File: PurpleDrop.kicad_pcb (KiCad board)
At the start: 4 copper layers, 161 x 92 mm, 145 parts, among them J1 Conn_02x32_Odd_Even, J2 Conn_02x32_Odd_Even, J3 Conn_02x20_Odd_Even, J4 Conn_01x04, J5 Conn_01x04, J6 Conn_01x04, J7 Conn_02x04_Odd_Even, J8 Conn_02x10_Odd_Even, J9 Barrel_Jack_Switch, Q1 SSM3K329R, Q2 SSM3K329R, Q3 SSM3K329R, Q4 SSM3K329R, SW1 SW_SPDT, U1 HV507, U10 RRE04EA6DFH, U11 RRE04EA6DFH, U12 RRE04EA6DFH, U13 RRE04EA6DFH, U14 RRE04EA6DFH, U15 RRE04EA6DFH, U16 RRE04EA6DFH, U17 RRE04EA6DFH, U18 RRE04EA6DFH, U19 RRE04EA6DFH, U2 HV507, U20 RRE04EA6DFH, U21 RRE04EA6DFH, U22 RRE04EA6DFH, U23 RRE04EA6DFH, U24 RRE04EA6DFH, U25 RRE04EA6DFH, U26 RRE04EA6DFH, U27 RRE04EA6DFH, U28 RRE04EA6DFH, U29 RRE04EA6DFH, U3 RRE04EA6DFH, U30 RRE04EA6DFH, U31 RRE04EA6DFH, U32 RRE04EA6DFH, U33 RRE04EA6DFH, U34 RRE04EA6DFH, U35 RRE04EA6DFH, U36 RRE04EA6DFH, U37 RRE04EA6DFH, U38 RRE04EA6DFH, U39 RRE04EA6DFH, U4 RRE04EA6DFH, U40 RRE04EA6DFH, U41 RRE04EA6DFH, U42 RRE04EA6DFH, U43 RRE04EA6DFH, U44 RRE04EA6DFH, U45 RRE04EA6DFH, U46 RRE04EA6DFH, U47 RRE04EA6DFH, U48 RRE04EA6DFH, U49 RRE04EA6DFH, U5 RRE04EA6DFH, U50 RRE04EA6DFH, U51 RRE04EA6DFH, U52 RRE04EA6DFH, U53 RRE04EA6DFH, U54 RRE04EA6DFH, U55 RRE04EA6DFH, U56 RRE04EA6DFH, U57 RRE04EA6DFH, U58 RRE04EA6DFH, U59 RRE04EA6DFH, U6 RRE04EA6DFH, U60 RRE04EA6DFH, U61 RRE04EA6DFH, U62 RRE04EA6DFH, U63 RRE04EA6DFH, U64 RRE04EA6DFH, U65 RRE04EA6DFH, U66 RRE04EA6DFH, U67 74LVC2T45DCT, U68 74LVC2T45DCT, U69 74LVC2T45DCT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

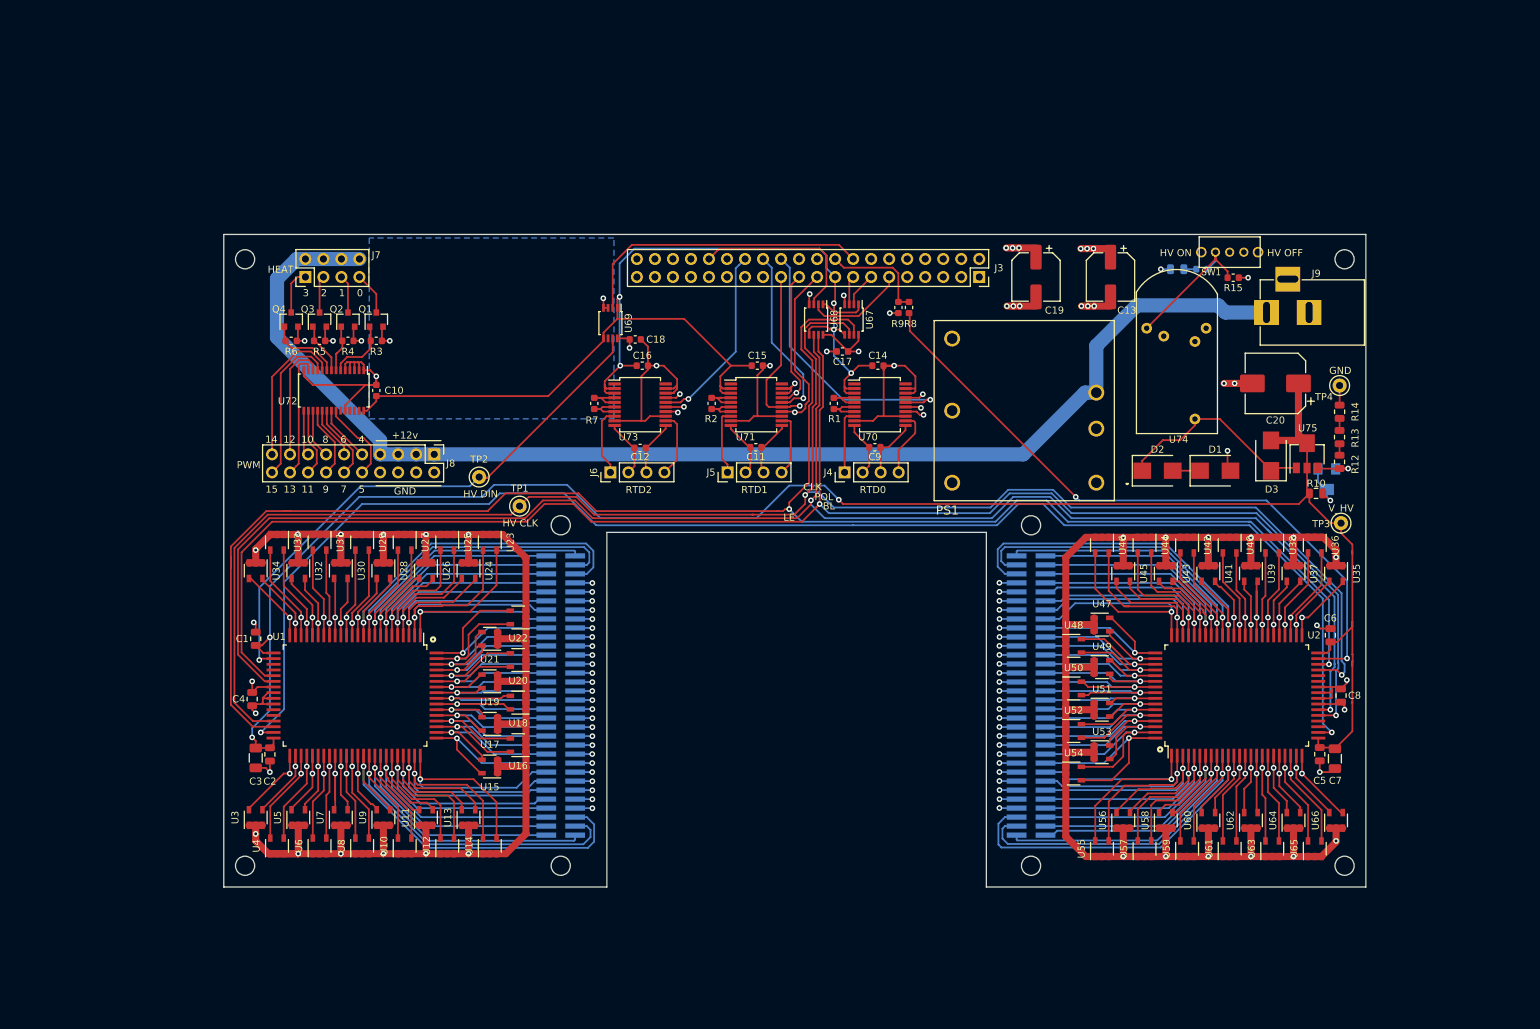
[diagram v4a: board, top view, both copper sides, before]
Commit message: fixes: added shunt, added HV power up, added default state to level shifters
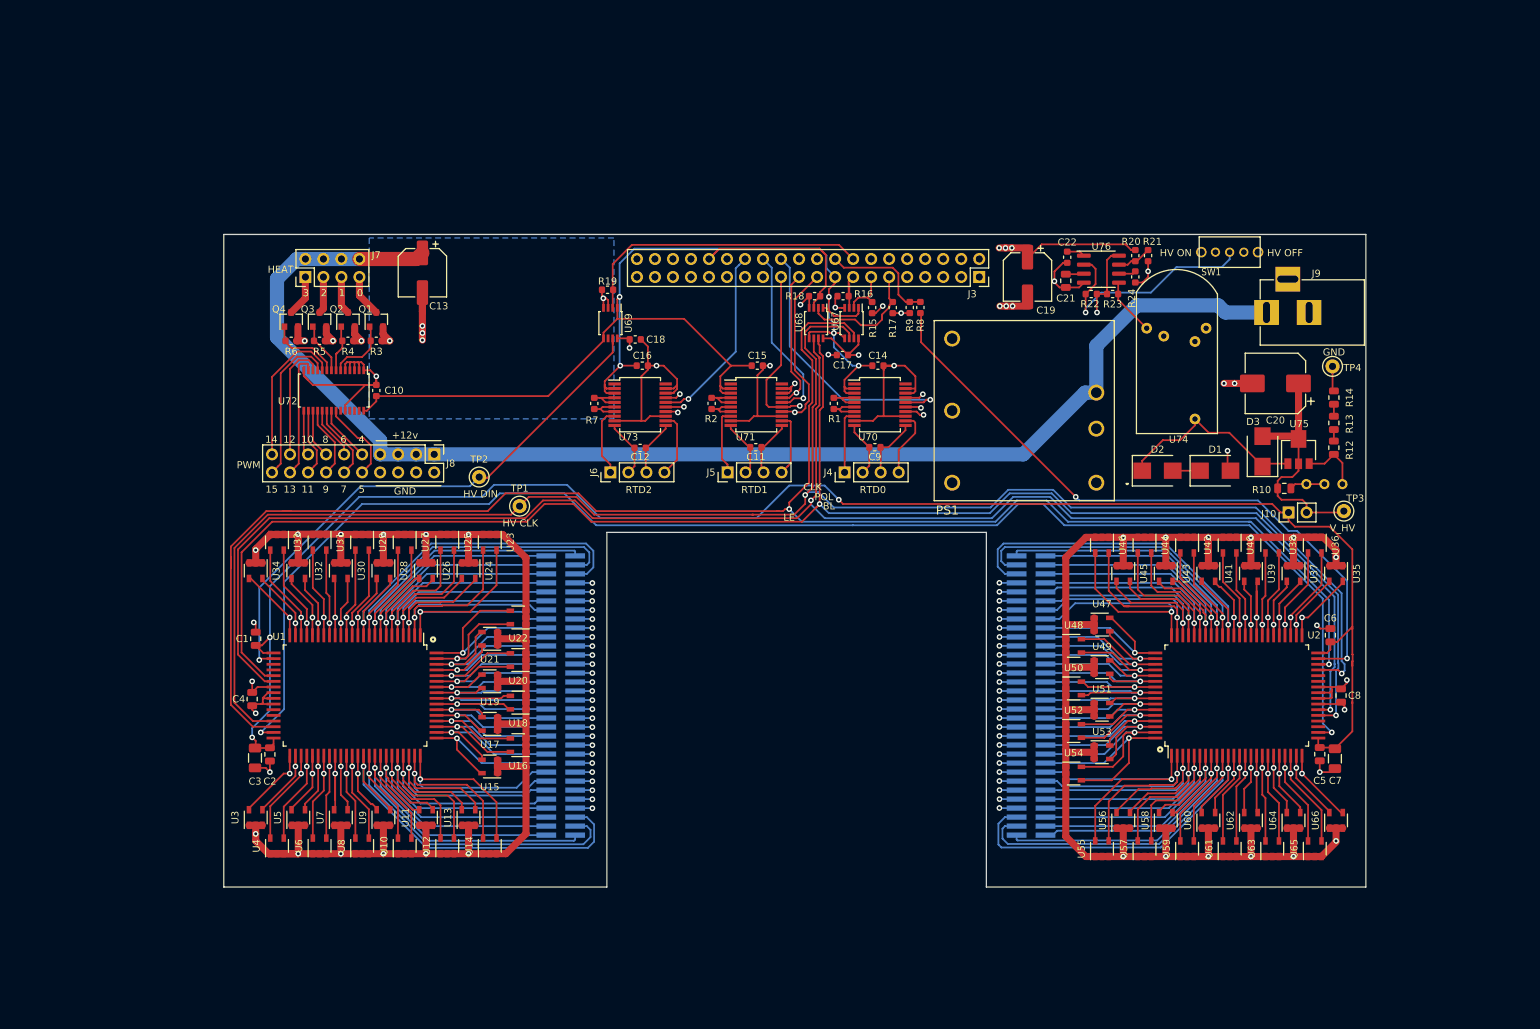
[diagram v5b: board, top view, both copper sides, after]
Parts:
- removed D4: LED_Small, LED_SMD:LED_0805_2012Metric
- removed REF** (x8): MountingHole_2.7mm_M2.5_ISO14580, MountingHole:MountingHole_2.7mm_M2.5_ISO14580
- removed Ref**: Val**, logos:purpledrop
- removed Ref**: Val**, logos:wlogo
- removed Ref**: Val**, logos:misl-logo
- added C21: 4.7uF, Capacitor_SMD:C_0805_2012Metric, F.Cu at (191.2, 61.5)
- added C22: 0.1uF, Capacitor_SMD:C_0603_1608Metric, F.Cu at (191.4, 58.2)
- added J10: current shunt, Connector_PinHeader_2.54mm:PinHeader_1x02_P2.54mm_Vertical, F.Cu at (222.6, 94.2)
- added R17: 10k, Resistor_SMD:R_0603_1608Metric, F.Cu at (166.8, 65.3)
- added R18: 10k, Resistor_SMD:R_0603_1608Metric, F.Cu at (155.8, 63.7)
- added R19: 10k, Resistor_SMD:R_0603_1608Metric, F.Cu at (126.6, 62.8)
- added R20: 16.5k, Resistor_SMD:R_0603_1608Metric, F.Cu at (201.0, 58.0)
- added R21: 18.7k, Resistor_SMD:R_0603_1608Metric, F.Cu at (202.8, 58.0)
- added R22: 10k, Resistor_SMD:R_0603_1608Metric, F.Cu at (194.8, 63.4)
- added R23: 10k, Resistor_SMD:R_0603_1608Metric, F.Cu at (197.8, 63.4)
- added R24: 10k, Resistor_SMD:R_0603_1608Metric, F.Cu at (201.0, 61.0)
- added U76: TL7702B, Package_SO:SOIC-8_3.9x4.9mm_P1.27mm, F.Cu at (196.2, 59.9)
- D1, D2: value 200v -> 180v
- R11: footprint Potentiometers:Potentiometer_Trimmer_Bourns_3214W -> Potentiometer_THT:Potentiometer_Bourns_3296W_Vertical
- R16: moved to F.Cu
- moved C13 97.0 mm to (100.5, 60.4)
- moved R15 51.1 mm to (163.9, 65.3), turned to 270 degrees
- moved R16 50.7 mm to (159.8, 63.7), turned to 180 degrees
- moved R10 4.54 mm to (222.0, 90.8)
- moved R11 2.96 mm to (225.1, 90.2)
- moved TP4 2.88 mm to (228.8, 73.6)
- moved R14 2.15 mm to (229.0, 78.0)
- moved R12 2.15 mm to (229.0, 85.1)
- moved R13 2.15 mm to (229.0, 81.6)
- moved TP3 1.75 mm to (230.4, 94.0)
- moved R8 1.60 mm to (170.7, 65.3)
- moved R9 1.60 mm to (169.2, 65.3)
- moved U75 1.34 mm to (224.0, 85.8)
- moved D3 1.34 mm to (218.9, 85.6)
- moved C19 1.20 mm to (185.8, 61.0)
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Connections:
- C20 pad 1: V_HV -> Net-(C20-Pad1)
- D3 pad 2: V_HV -> Net-(C20-Pad1)
- R10 pad 1: V_HV -> Net-(C20-Pad1)
- R15 pad 1: GND -> /pi interface/pi_latch
- R15 pad 2: Net-(R15-Pad2) -> GND
- R16 pad 1: Net-(D4-Pad2) -> /pi interface/pi_clk
- R16 pad 2: Net-(R15-Pad2) -> GND
- SW1 pad 1: Net-(R15-Pad2) -> Net-(SW1-Pad1)
- SW1 pad 2: +12V -> Net-(R22-Pad1)
- SW1 pad 3: Net-(SW1-Pad3) -> GND
- TP3 pad 1: V_HV -> Net-(C20-Pad1)
- U74 pad 5: Net-(R15-Pad2) -> /power/HV_CNTRL
- U75 pad 2: V_HV -> Net-(C20-Pad1)
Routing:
- net Net-(C20-Pad1): track 0.00 -> 34.3 mm
- net Net-(R22-Pad1): track 0.00 -> 33.4 mm, vias 0 -> 1
- net GND: track 608.3 -> 640.6 mm, vias 55 -> 56
- net V_HV: track 266.2 -> 241.5 mm
- net Net-(R15-Pad2): track 22.4 -> 0.00 mm
- net +5V: track 25.6 -> 41.7 mm
- net +12V: track 185.7 -> 201.5 mm, vias 3 -> 1
- net /power/HV_CNTRL: track 0.00 -> 8.12 mm
- net Net-(R20-Pad1): track 0.00 -> 4.96 mm
- net /pi interface/pi_blank: track 14.1 -> 17.8 mm
- net /pi interface/pi_pol: track 25.2 -> 28.2 mm
- net /pi interface/pi_clk: track 4.08 -> 7.04 mm
- net Net-(R11-Pad3): track 6.25 -> 9.02 mm, vias 1 -> 0
- net Net-(C22-Pad1): track 0.00 -> 2.58 mm
- net Net-(C21-Pad1): track 0.00 -> 2.57 mm
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
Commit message: changed designators for tidyness sake.
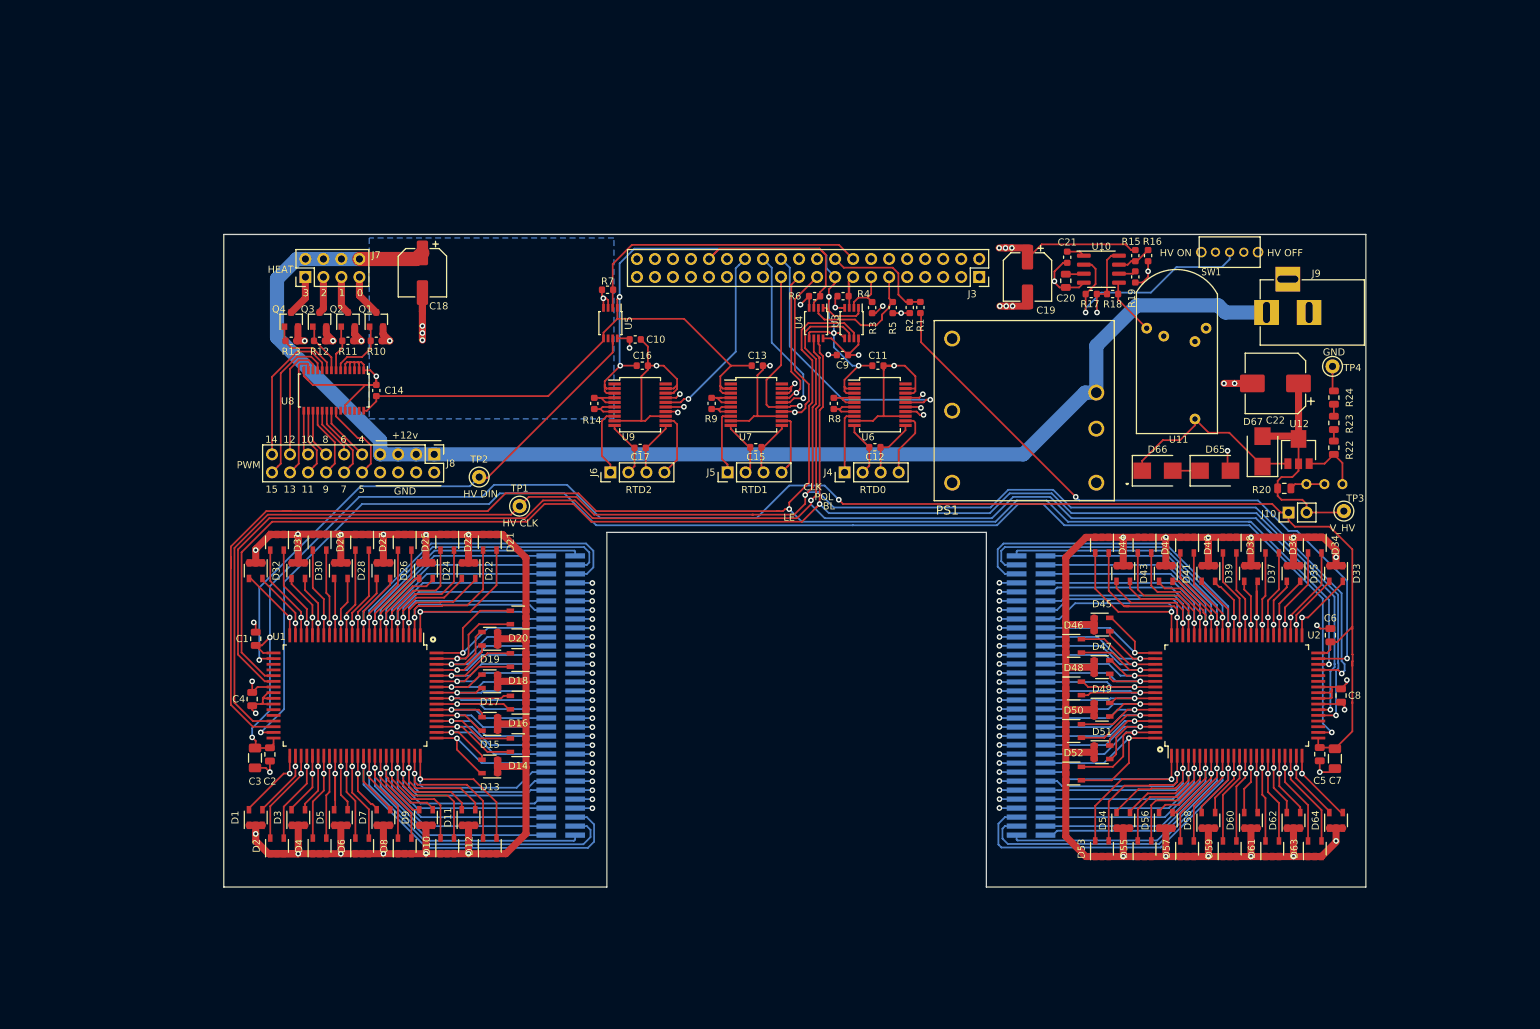
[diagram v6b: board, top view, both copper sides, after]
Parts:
- renumbered C18 to C10, C14 to C11, C9 to C12, C15 to C13, C10 to C14, C11 to C15, C12 to C17, C13 to C18, C21 to C20, C22 to C21, C20 to C22, C17 to C9, U3 to D1, U12 to D10, U13 to D11, U14 to D12, U15 to D13, U16 to D14, U17 to D15, U18 to D16, U19 to D17, U20 to D18, U21 to D19, U4 to D2, U22 to D20, U23 to D21, U24 to D22, U25 to D23, U26 to D24, U27 to D25, U28 to D26, U29 to D27, U30 to D28, U31 to D29, U5 to D3, U32 to D30, U33 to D31, U34 to D32, U35 to D33, U36 to D34, U37 to D35, U38 to D36, U39 to D37, U40 to D38, U41 to D39, U6 to D4, U42 to D40, U43 to D41, U44 to D42, U45 to D43, U46 to D44, U47 to D45, U48 to D46, U49 to D47, U50 to D48, U51 to D49, U7 to D5, U52 to D50, U53 to D51, U54 to D52, U55 to D53, U56 to D54, U57 to D55, U58 to D56, U59 to D57, U60 to D58, U61 to D59, U8 to D6, U62 to D60, U63 to D61, U64 to D62, U65 to D63, U66 to D64, D1 to D65, D2 to D66, D3 to D67, U9 to D7, U10 to D8, U11 to D9, R8 to R1, R3 to R10, R4 to R11, R5 to R12, R6 to R13, R7 to R14, R20 to R15, R21 to R16, R22 to R17, R23 to R18, R24 to R19, R9 to R2, R10 to R20, R11 to R21, R12 to R22, R13 to R23, R14 to R24, R15 to R3, R16 to R4, R17 to R5, R18 to R6, R19 to R7, R1 to R8, R2 to R9, U76 to U10, U74 to U11, U75 to U12, U67 to U3, U68 to U4, U69 to U5, U70 to U6, U71 to U7, U72 to U8, U73 to U9

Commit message: minor annotation and cleanup
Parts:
- renumbered U11 to PS1, PS1 to PS2, U12 to U11

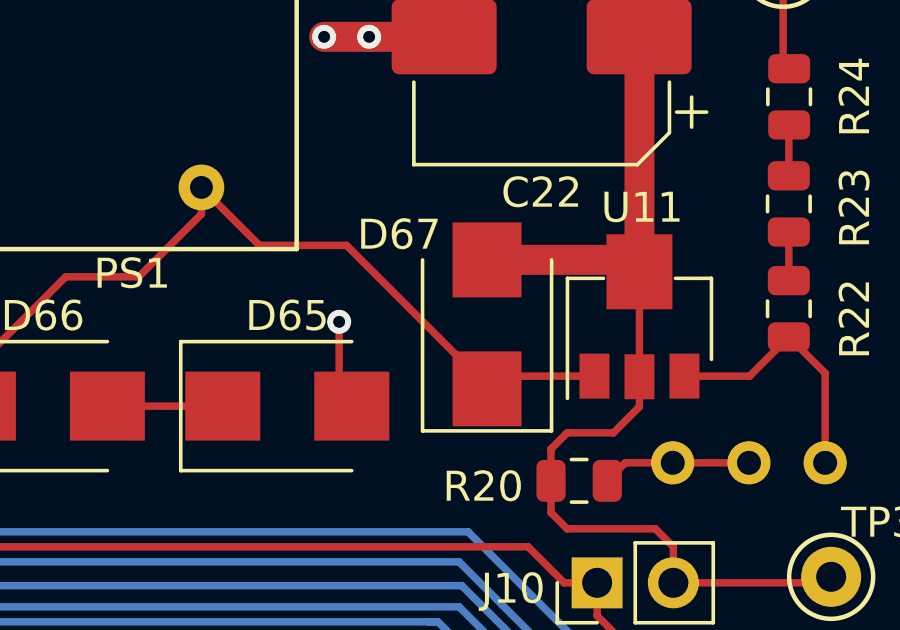
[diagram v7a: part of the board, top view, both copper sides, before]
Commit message: small tweaks and PN field added to most part
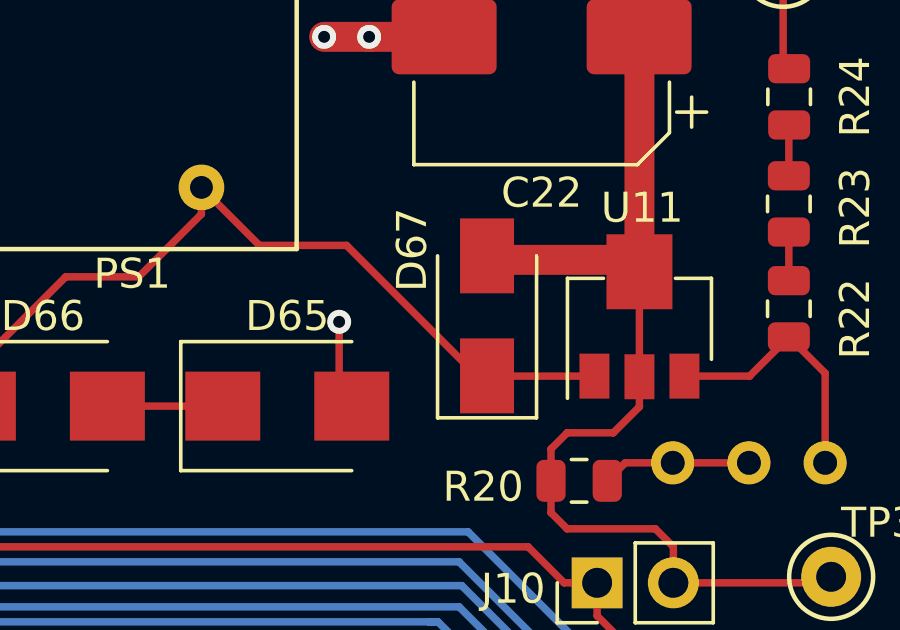
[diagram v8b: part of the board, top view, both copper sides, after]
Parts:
- D67: footprint Diode_SMD:D_SMB -> Diode_SMD:D_SMA
- moved D67 0.28 mm to (218.9, 85.3)
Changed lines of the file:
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@@
     (solder_mask_min_width 0.25)
     (aux_axis_origin 0 0)
-    (visible_elements 7FFFFF7F)
+    (visible_elements 7FF5FF7F)
     (pcbplotparams
       (layerselection 0x010fc_ffffffff)
@@
     (add_net pi_SCK_0)
   )
+  (module Diode_SMD:D_SMA (layer F.Cu)
+    (at 218.93 85.3 90)
+    (descr "Diode SMA (DO-214AC)")
+    (tags "Diode SMA (DO-214AC)")
+    (attr smd)
+    (fp_text reference D67 (at 2.2 -2.5 90) (layer F.SilkS)
+      (effects (font (size 1 1) (thickness 0.15)))
+    )
+    (fp_text value D_Small (at 0 2.6 90) (layer F.Fab)
+      (effects (font (size 1 1) (thickness 0.15)))
+    )
+    (fp_line (start -3.4 -1.65) (end 2 -1.65) (layer F.SilkS) (width 0.12))
+    (fp_line (start -3.4 1.65) (end 2 1.65) (layer F.SilkS) (width 0.12))
+    (fp_line (start -0.64944 0.00102) (end 0.50118 -0.79908) (layer F.Fab) (width 0.1))
+    (fp_line (start -0.64944 0.00102) (end 0.50118 0.75032) (layer F.Fab) (width 0.1))
+    (fp_line (start 0.50118 0.75032) (end 0.50118 -0.79908) (layer F.Fab) (width 0.1))
+    (fp_line (start -0.64944 -0.79908) (end -0.64944 0.80112) (layer F.Fab) (width 0.1))
+    (fp_line (start 0.50118 0.00102) (end 1.4994 0.00102) (layer F.Fab) (width 0.1))
+    (fp_line (start -0.64944 0.00102) (end -1.55114 0.00102) (layer F.Fab) (width 0.1))
+    (fp_line (start -3.5 1.75) (end -3.5 -1.75) (layer F.CrtYd) (width 0.05))
+    (fp_line (start 3.5 1.75) (end -3.5 1.75) (layer F.CrtYd) (width 0.05))
+    (fp_line (start 3.5 -1.75) (end 3.5 1.75) (layer F.CrtYd) (width 0.05))
+    (fp_line (start -3.5 -1.75) (end 3.5 -1.75) (layer F.CrtYd) (width 0.05))
+    (fp_line (start 2.3 -1.5) (end -2.3 -1.5) (layer F.Fab) (width 0.1))
+    (fp_line (start 2.3 -1.5) (end 2.3 1.5) (layer F.Fab) (width 0.1))
+    (fp_line (start -2.3 1.5) (end -2.3 -1.5) (layer F.Fab) (width 0.1))
+    (fp_line (start 2.3 1.5) (end -2.3 1.5) (layer F.Fab) (width 0.1))
+    (fp_line (start -3.4 -1.65) (end -3.4 1.65) (layer F.SilkS) (width 0.12))
+    (fp_text user %R (at 0 -2.5 90) (layer F.Fab)
+      (effects (font (size 1 1) (thickness 0.15)))
+    )
+    (pad 2 smd rect (at 2 0 90) (size 2.5 1.8) (layers F.Cu F.Paste F.Mask)
+      (net 211 "Net-(C22-Pad1)"))
+    (pad 1 smd rect (at -2 0 90) (size 2.5 1.8) (layers F.Cu F.Paste F.Mask)
+      (net 219 "Net-(D66-Pad1)"))
+    (model ${KISYS3DMOD}/Diode_SMD.3dshapes/D_SMA.wrl
+      (at (xyz 0 0 0))
+      (scale (xyz 1 1 1))
+      (rotate (xyz 0 0 0))
+    )
+  )
   (module Capacitor_SMD:CP_Elec_6.3x5.9 (layer F.Cu)
     (at 100.5 60.4 270)
@@
       (net 219 "Net-(D66-Pad1)"))
     (model ${KISYS3DMOD}/Diode_SMD.3dshapes/D_SMB.wrl
-      (at (xyz 0 0 0))
-      (scale (xyz 1 1 1))
-      (rotate (xyz 0 0 0))
-    )
-  )
-  (module Diode_SMD:D_SMB (layer F.Cu)
-    (at 218.93 85.585 90)
-    (descr "Diode SMB (DO-214AA)")
-    (tags "Diode SMB (DO-214AA)")
-    (attr smd)
-    (fp_text reference D67 (at 2.985 -2.93 180) (layer F.SilkS)
-      (effects (font (size 1 1) (thickness 0.15)))
-    )
-    (fp_text value D_Small (at 0 3.1 90) (layer F.Fab)
-      (effects (font (size 1 1) (thickness 0.15)))
-    )
-    (fp_line (start -3.55 -2.15) (end 2.15 -2.15) (layer F.SilkS) (width 0.12))
-    (fp_line (start -3.55 2.15) (end 2.15 2.15) (layer F.SilkS) (width 0.12))
-    (fp_line (start -0.64944 0.00102) (end 0.50118 -0.79908) (layer F.Fab) (width 0.1))
-    (fp_line (start -0.64944 0.00102) (end 0.50118 0.75032) (layer F.Fab) (width 0.1))
-    (fp_line (start 0.50118 0.75032) (end 0.50118 -0.79908) (layer F.Fab) (width 0.1))
-    (fp_line (start -0.64944 -0.79908) (end -0.64944 0.80112) (layer F.Fab) (width 0.1))
-    (fp_line (start 0.50118 0.00102) (end 1.4994 0.00102) (layer F.Fab) (width 0.1))
-    (fp_line (start -0.64944 0.00102) (end -1.55114 0.00102) (layer F.Fab) (width 0.1))
-    (fp_line (start -3.65 2.25) (end -3.65 -2.25) (layer F.CrtYd) (width 0.05))
-    (fp_line (start 3.65 2.25) (end -3.65 2.25) (layer F.CrtYd) (width 0.05))
-    (fp_line (start 3.65 -2.25) (end 3.65 2.25) (layer F.CrtYd) (width 0.05))
-    (fp_line (start -3.65 -2.25) (end 3.65 -2.25) (layer F.CrtYd) (width 0.05))
-    (fp_line (start 2.3 -2) (end -2.3 -2) (layer F.Fab) (width 0.1))
-    (fp_line (start 2.3 -2) (end 2.3 2) (layer F.Fab) (width 0.1))
-    (fp_line (start -2.3 2) (end -2.3 -2) (layer F.Fab) (width 0.1))
-    (fp_line (start 2.3 2) (end -2.3 2) (layer F.Fab) (width 0.1))
-    (fp_line (start -3.55 -2.15) (end -3.55 2.15) (layer F.SilkS) (width 0.12))
-    (fp_text user %R (at 0 -3 90) (layer F.Fab)
-      (effects (font (size 1 1) (thickness 0.15)))
-    )
-    (pad 2 smd rect (at 2.15 0 90) (size 2.5 2.3) (layers F.Cu F.Paste F.Mask)
-      (net 211 "Net-(C22-Pad1)"))
-    (pad 1 smd rect (at -2.15 0 90) (size 2.5 2.3) (layers F.Cu F.Paste F.Mask)
-      (net 219 "Net-(D66-Pad1)"))
-    (model ${KISYS3DMOD}/Diode_SMD.3dshapes/D_SMB.wrl
